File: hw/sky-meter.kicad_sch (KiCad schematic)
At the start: 60 parts, among them J1 TYPE-C-31-M-12, J11 battery, J3 battery, J6 A, J7 display, J8 K, Q2 ML5203, Q5 ML5203, SW1 btn-up, SW2 btn-sel, SW3 btn-down, U11 MCP73831, U2 ME6216A33XG, U3 BMP280, U4 STM32G431CBUx, U5 PCF8563T, Y1 32768, Y1 NX3215SA 32.768K, Y2 XTAL3225 8MHz

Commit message: hm - доработана схема
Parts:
- removed C5: 22pF, Capacitor_SMD:C_0805_2012Metric, symbol Device:C
- removed Q2: ML5203, Package_TO_SOT_SMD:SOT-23, symbol Device:Q_PMOS_GSD
- removed R10: 510, Resistor_SMD:R_0603_1608Metric, symbol Device:R
- removed R7: 100k, Resistor_SMD:R_0603_1608Metric, symbol Device:R
- removed U5: PCF8563T, Package_SO:SOIC-8_3.9x4.9mm_P1.27mm, symbol Timer_RTC:PCF8563T
- removed Y1: 32768, Crystal:Crystal_AT310_D3.0mm_L10.0mm_Vertical, symbol Device:Crystal
- added D1 (x2): 1N5819, Diode_SMD:D_SOD-323, symbol Device:D
- added Q111 (x2): ML2502, Package_TO_SOT_SMD:SOT-23, symbol Device:Q_NMOS_GSD
- added R112 (x2): 510, Resistor_SMD:R_0805_2012Metric, symbol Device:R
- added R113: 3k3, Resistor_SMD:R_0805_2012Metric, symbol Device:R
- added R113 (x2): 100k, Resistor_SMD:R_0805_2012Metric, symbol Device:R
- added R6: 0, Resistor_SMD:R_0603_1608Metric, symbol Device:R
- C4: footprint Capacitor_THT:CP_Radial_D4.0mm_P1.50mm -> Capacitor_Tantalum_SMD:CP_EIA-7343-20_Kemet-V
- L1: footprint (none) -> Inductor_SMD:L_0603_1608Metric
- R25: value 2k2 -> 4k7
- Y1: footprint (none) -> NX3215SA-32.768K-STD-MUA-14:XTAL_NX3215SA-32.768K-STD-MUA-14
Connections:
- net +BATT: now also R13.2, D1.2 (A), R6.2; no longer C21.1, U11.3 (VBAT)
- net GND: now also Q111.2 (S), Q111.2 (S), R113.2, R113.2; no longer J8.1 (Pin_1)
- net chg-cur: now also R113.1
- net d-led: now also R112.2
- net hwen: now also U4.22 (PB10); no longer U4.25 (PB12)
- net usb-5v: now also D1.2 (A); no longer C22.1, U2.3 (VI)
- new net: Q111.1 (G), R112.1, R113.1 (x2)
- new net: C22.1, D1.1 (K), D1.1 (K), U2.3 (VI)
- new net: C21.1, R6.1, U11.3 (VBAT)
- new net: J8.1 (Pin_1), Q111.3 (D)
- new net: Q111.3 (D), R113.2
- new net chg-hi: R112.2, U4.25 (PB12)
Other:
- moved on the sheet: C14, C15, C17, C18, C19, C20, C21, C22, C23, C27, C4, C5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

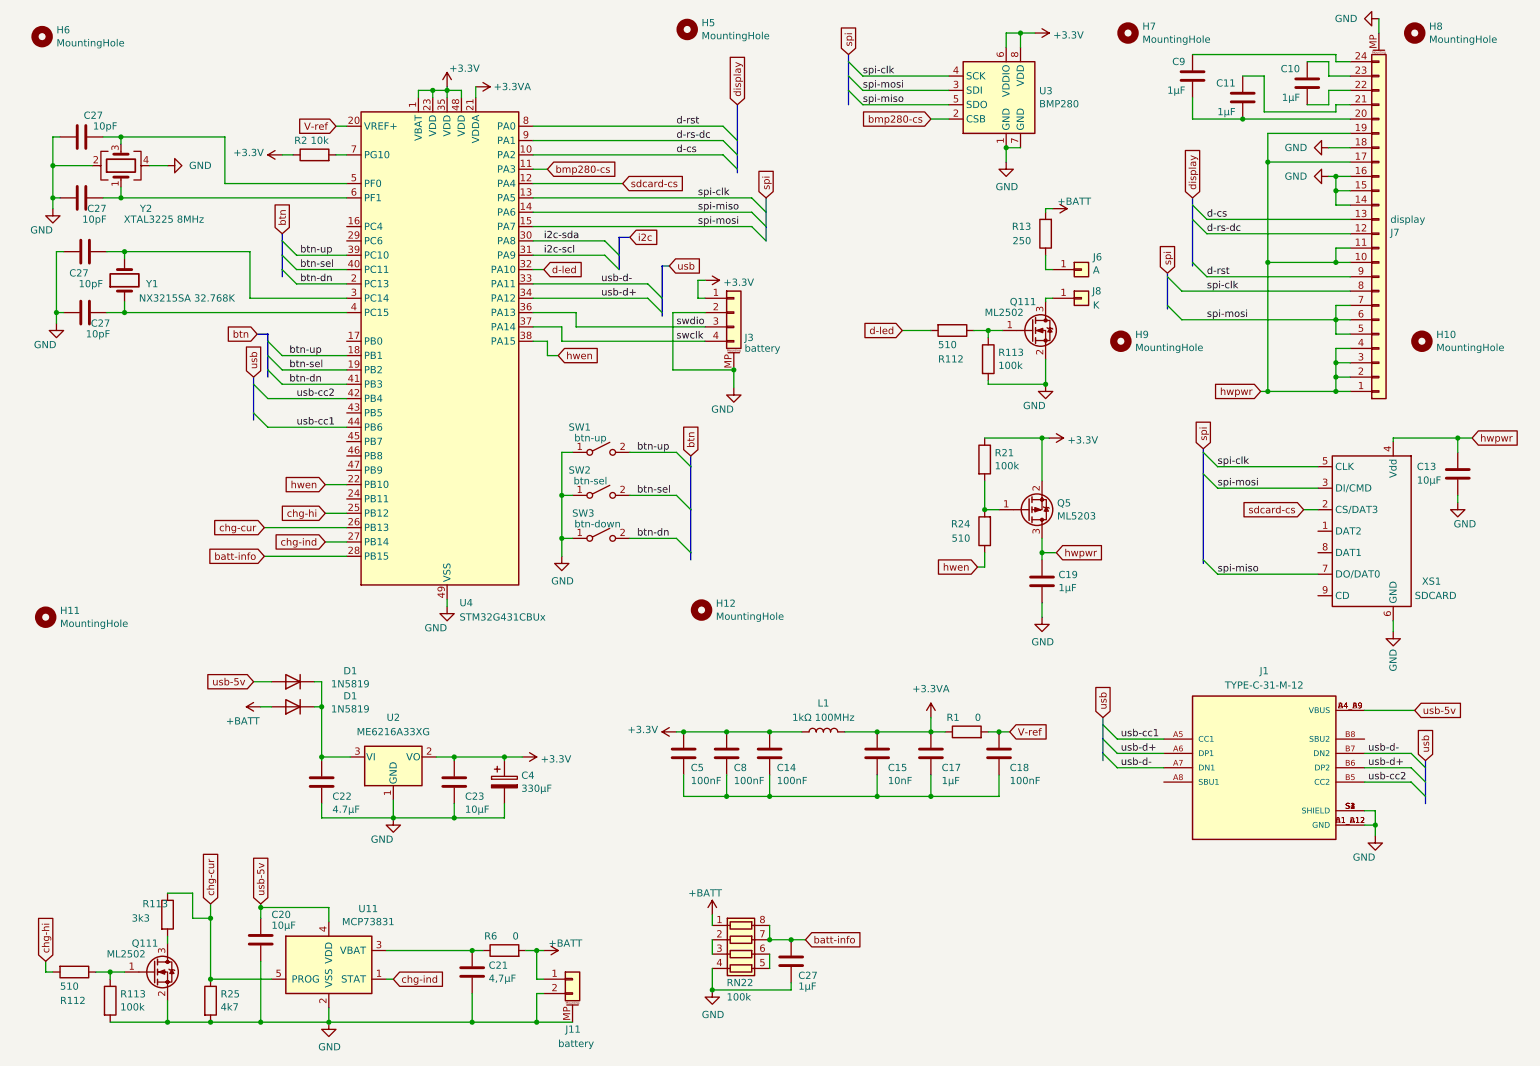
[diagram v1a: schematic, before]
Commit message: разведена плата, надо проверять
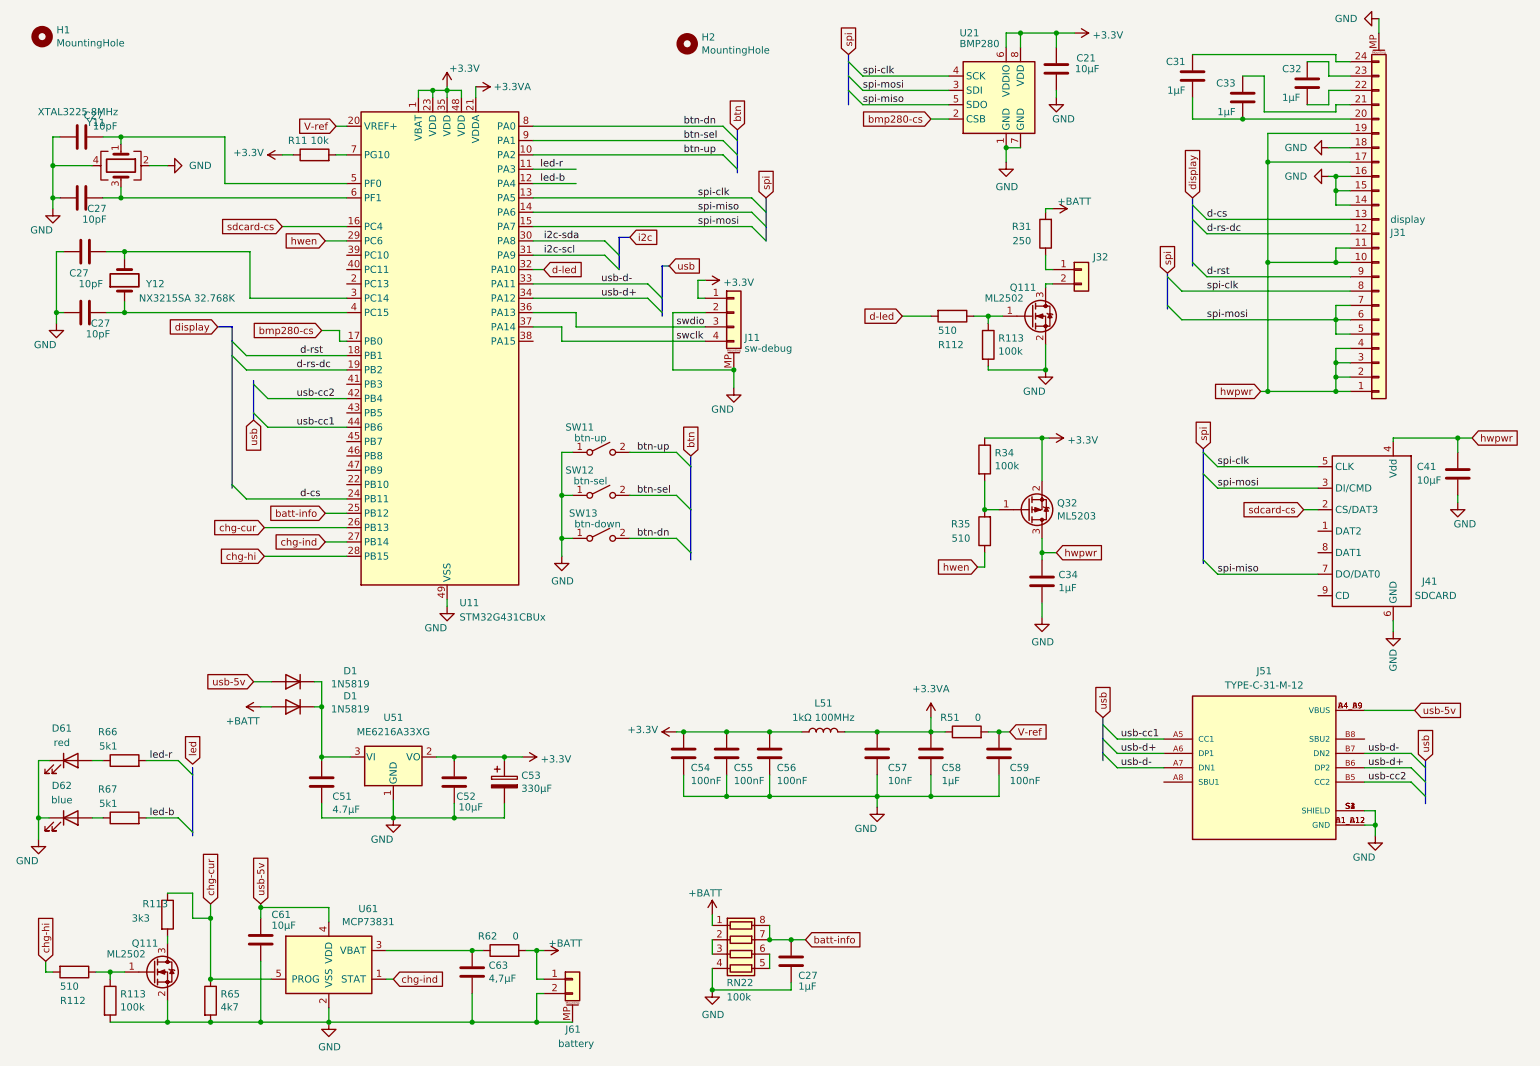
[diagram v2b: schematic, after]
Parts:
- removed H10, H9: MountingHole, MHole:MountingHole_1.5, symbol Mechanical:MountingHole
- removed H11, H12: MountingHole, MountingHole:MountingHole_3.2mm_M3, symbol Mechanical:MountingHole
- removed H7, H8: MountingHole, MountingHole:MountingHole_2.2mm_M2, symbol Mechanical:MountingHole
- removed J8: K, Connector_Wire:SolderWire-1sqmm_1x01_D1.4mm_OD2.7mm, symbol Connector_Generic:Conn_01x01
- added C21: 10μF, Capacitor_SMD:C_0603_1608Metric, symbol Device:C
- added D61: red, LED_SMD:LED_0603_1608Metric, symbol Device:LED
- added D62: blue, LED_SMD:LED_0603_1608Metric, symbol Device:LED
- added R66, R67: 5k1, Resistor_SMD:R_0603_1608Metric, symbol Device:R
- J11: renamed from J3; value battery -> sw-debug; footprint Connector_Molex:Molex_PicoBlade_53261-0271_1x02-1MP_P1.25mm_Horizontal -> Connector_Molex:Molex_PicoBlade_53398-0471_1x04-1MP_P1.25mm_Vertical
- J32: renamed from J6; value A -> ~; footprint Connector_Wire:SolderWire-1sqmm_1x01_D1.4mm_OD2.7mm -> my:display-256x192; symbol Connector_Generic:Conn_01x01 -> Connector_Generic:Conn_01x02
- R112, R113: footprint Resistor_SMD:R_0805_2012Metric -> Resistor_SMD:R_0603_1608Metric
- R31: renamed from R13; footprint Resistor_SMD:R_0603_1608Metric -> Resistor_SMD:R_0805_2012Metric
- renumbered C9 to C31, C10 to C32, C11 to C33, C19 to C34, C13 to C41, C22 to C51, C23 to C52, C4 to C53, C5 to C54, C8 to C55, C14 to C56, C15 to C57, C17 to C58, C18 to C59, C20 to C61, C21 to C63, H6 to H1, H5 to H2, J7 to J31, XS1 to J41, J1 to J51, J11 to J61, L1 to L51, Q5 to Q32, R2 to R11, R21 to R34, R24 to R35, R1 to R51, R6 to R62, R25 to R65, SW1 to SW11, SW2 to SW12, SW3 to SW13, U4 to U11, U3 to U21, U2 to U51, U11 to U61, Y2 to Y11, Y1 to Y12
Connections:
- net +3V3: now also C52.2, C21.1; no longer C52.1
- net GND: now also C52.1, C54.2, C55.2, C56.2, C57.2, C58.2, C59.2, C21.2, D61.1 (K), D62.1 (K); no longer C52.2
- net batt-info: now also U11.25 (PB12); no longer U11.28 (PB15)
- net bmp280-cs: now also U11.17 (PB0); no longer U11.11 (PA3)
- net btn-dn: now also U11.8 (PA0); no longer U11.2 (PC13), U11.41 (PB3)
- net btn-sel: now also U11.9 (PA1); no longer U11.19 (PB2), U11.40 (PC11)
- net btn-up: now also U11.10 (PA2); no longer U11.18 (PB1), U11.39 (PC10)
- net chg-hi: now also U11.28 (PB15); no longer U11.25 (PB12)
- net d-cs: now also U11.24 (PB11); no longer U11.10 (PA2)
- net d-rs-dc: now also U11.19 (PB2); no longer U11.9 (PA1)
- net d-rst: now also U11.18 (PB1); no longer U11.8 (PA0)
- net hwen: now also U11.29 (PC6); no longer U11.22 (PB10), U11.38 (PA15)
- net sdcard-cs: now also U11.16 (PC4); no longer U11.12 (PA4)
- net at C32.1: now also J31.23 (Pin_23); no longer J31.22 (Pin_22)
- net at C32.2: now also J31.22 (Pin_22); no longer J31.23 (Pin_23)
- net at Q111.3 (D): now also J32.2 (Pin_2)
- net at C27.2, U11.6 (PF1): now also Y11.3; no longer Y11.1
- net at C27.2, U11.5 (PF0): now also Y11.1; no longer Y11.3
- new net: D61.2 (A), R66.1
- new net: D62.2 (A), R67.1
- new net led-b: R67.2, U11.12 (PA4)
- new net led-r: R66.2, U11.11 (PA3)
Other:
- moved on the sheet: C32, C52, H2, Q111, R112, R113, Y11
